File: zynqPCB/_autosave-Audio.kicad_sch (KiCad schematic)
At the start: 8 parts, among them U20 xc7z020clg484

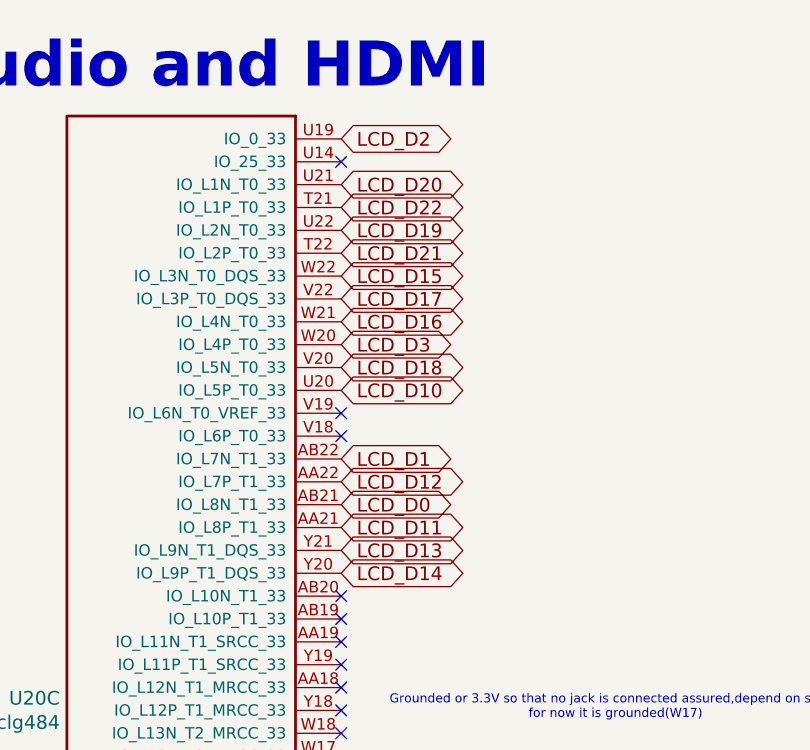
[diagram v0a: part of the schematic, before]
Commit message: removed grounded resistor can configure from the vivado and removed LCD
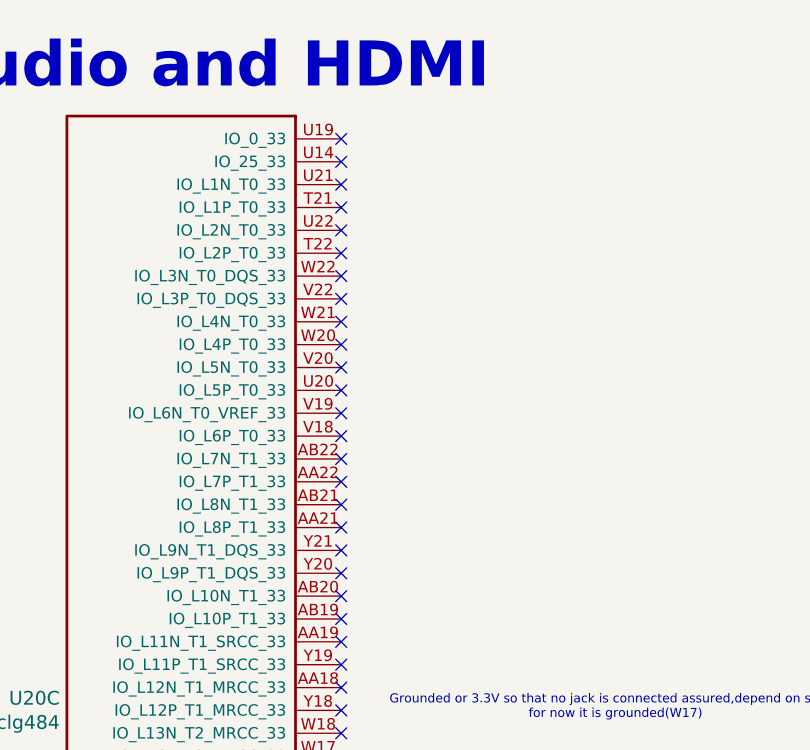
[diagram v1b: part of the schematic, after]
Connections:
- net LCD_D0: no longer names the net of U20.AB21 (IO_L8N_T1_33)
- net LCD_D1: no longer names the net of U20.AB22 (IO_L7N_T1_33)
- net LCD_D10: no longer names the net of U20.U20 (IO_L5P_T0_33)
- net LCD_D11: no longer names the net of U20.AA21 (IO_L8P_T1_33)
- net LCD_D12: no longer names the net of U20.AA22 (IO_L7P_T1_33)
- net LCD_D13: no longer names the net of U20.Y21 (IO_L9N_T1_DQS_33)
- net LCD_D14: no longer names the net of U20.Y20 (IO_L9P_T1_DQS_33)
- net LCD_D15: no longer names the net of U20.W22 (IO_L3N_T0_DQS_33)
- net LCD_D16: no longer names the net of U20.W21 (IO_L4N_T0_33)
- net LCD_D17: no longer names the net of U20.V22 (IO_L3P_T0_DQS_33)
- net LCD_D18: no longer names the net of U20.V20 (IO_L5N_T0_33)
- net LCD_D19: no longer names the net of U20.U22 (IO_L2N_T0_33)
- net LCD_D2: no longer names the net of U20.U19 (IO_0_33)
- net LCD_D20: no longer names the net of U20.U21 (IO_L1N_T0_33)
- net LCD_D21: no longer names the net of U20.T22 (IO_L2P_T0_33)
- net LCD_D22: no longer names the net of U20.T21 (IO_L1P_T0_33)
- net LCD_D3: no longer names the net of U20.W20 (IO_L4P_T0_33)
- no-connect marks 33 -> 50
